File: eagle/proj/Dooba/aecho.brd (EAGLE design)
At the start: 43.2 x 24.6 mm, 47 parts, among them J3 SJ1-3523N, P1 I2C(SCL-SDA), P2 MP3_CTL(SCKR-SDI-DREQ-RST), P3 AMP_CTL(SHDN-CLK-UPDN), P4 PWR(GND-VIN-GND), P9 AOUT_L-GND-AOUT_R, U10 CS4334, U11 LM4811PDSO-10, U12 5.0V, U7 3.3V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

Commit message: Redesigned ioNode using ATMEGA1284P, replaced esp8266 with ft232rq usb/serial
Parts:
- moved C25 8.62 mm to (44.5, 39.1)
- moved C30 8.62 mm to (44.5, 18.8)
- moved C31 8.62 mm to (51.1, 18.8)
- moved C34 8.62 mm to (52.6, 21.6)
- moved C37 8.62 mm to (44.5, 22.4)
- moved R11 8.62 mm to (47.8, 21.6)
- moved U7 8.62 mm to (47.0, 39.1)
- moved U9 8.62 mm to (50.3, 29.2)
- moved X2 8.62 mm to (47.8, 18.8)
- moved C42 8.62 mm to (30.5, 31.0)
- moved C44 8.62 mm to (30.5, 36.3)
- moved C47 8.62 mm to (23.1, 40.4)
- moved C48 8.62 mm to (25.1, 20.8)
- moved C49 8.62 mm to (25.1, 26.4)
- moved C51 8.62 mm to (27.9, 33.0)
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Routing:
- net GND: vias 92 -> 93

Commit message: Started designing Shiva mp3 player (new version)
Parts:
- moved C25 0.92 mm to (43.7, 39.6)
- moved C26 0.92 mm to (48.8, 39.6)
- moved C32 0.92 mm to (40.1, 30.0)
- moved C33 0.92 mm to (41.9, 30.0)
- moved C40 0.92 mm to (32.8, 35.1)
- moved C43 0.92 mm to (29.7, 33.3)
- moved C45 0.92 mm to (50.5, 39.6)
- moved C46 0.92 mm to (55.6, 39.6)
- moved C52 0.92 mm to (25.4, 39.1)
- moved J3 0.92 mm to (32.5, 21.8)
- moved P3 0.92 mm to (20.3, 27.9)
- moved P4 0.92 mm to (20.3, 35.6)
- moved P9 0.92 mm to (38.1, 40.6)
- moved R17 0.92 mm to (29.7, 35.1)
- moved R18 0.92 mm to (32.8, 33.3)
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
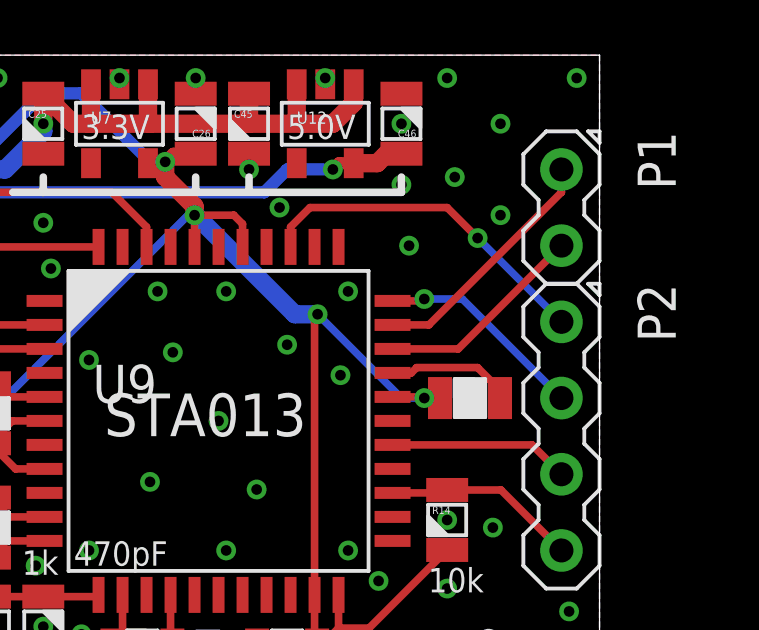
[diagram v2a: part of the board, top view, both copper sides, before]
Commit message: Fixed STA013 Device in Eagle Library Fixed Aecho Board to use updated STA013 Fixed ioNode Schematic (74125 buffers for USB UART had their !OE tied to VCC...)
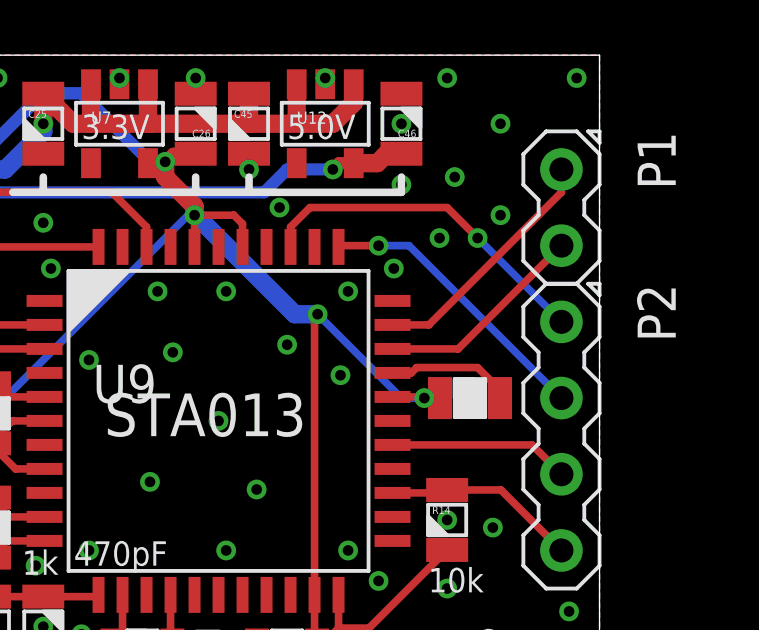
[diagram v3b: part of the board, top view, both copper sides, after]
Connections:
- net STA013_SDI: now also U9.34; no longer U9.33
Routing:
- net STA013_SDI: track 7.02 -> 9.55 mm
- net GND: vias 93 -> 94
